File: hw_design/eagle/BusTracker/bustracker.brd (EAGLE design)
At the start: 53.3 x 59.7 mm, 9 parts, among them J1 ARDUINO_R3_SHIELD

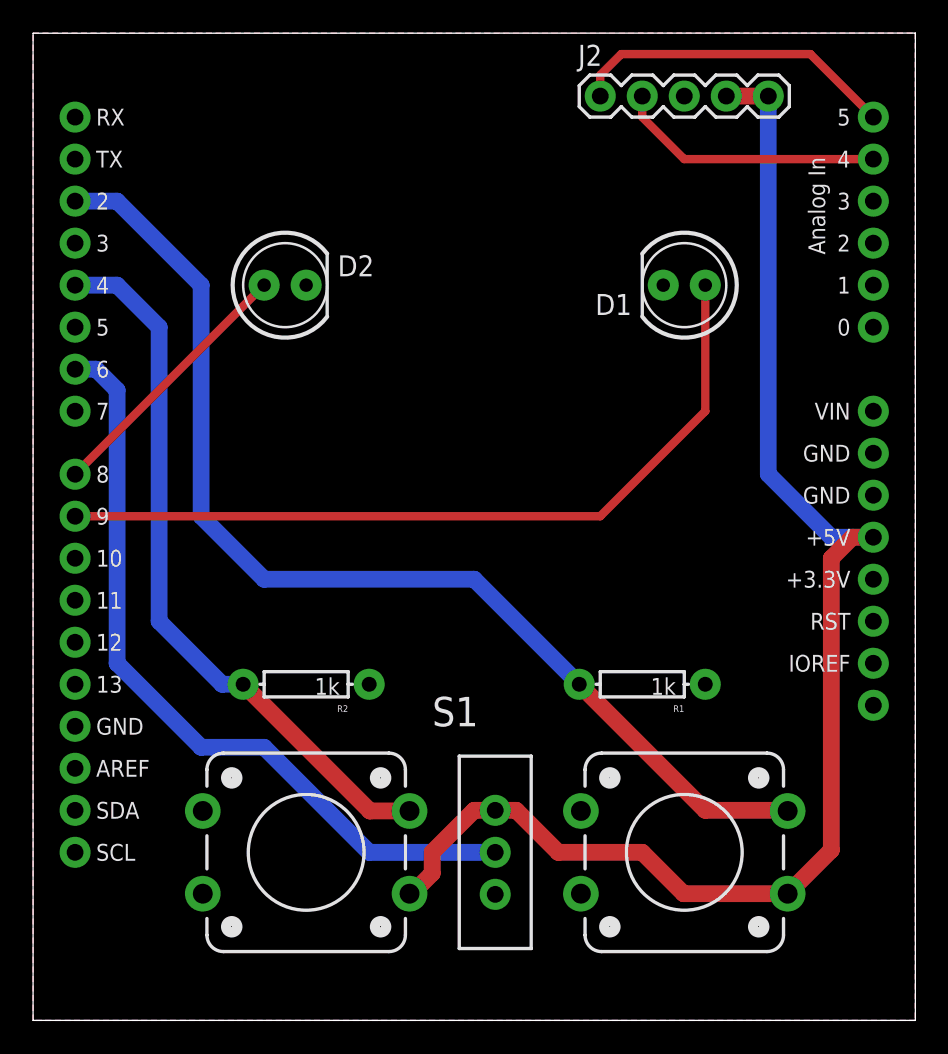
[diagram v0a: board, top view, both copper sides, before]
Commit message: Added silkscreen layer
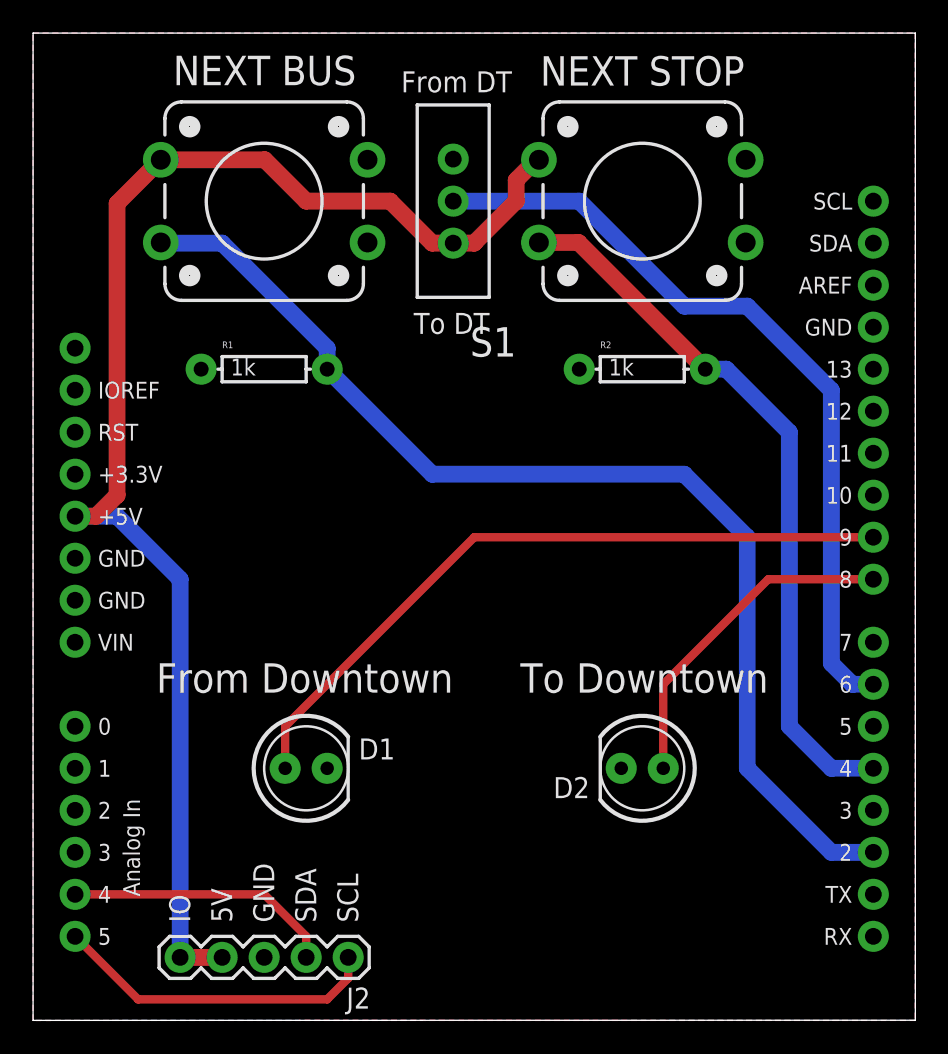
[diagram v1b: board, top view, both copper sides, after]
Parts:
- moved J1 80.1 mm to (53.3, 59.7), turned to 180 degrees
- moved J2 54.3 mm to (19.1, 3.81), turned to 180 degrees
- moved S2 46.9 mm to (14.0, 49.5), turned to 180 degrees
- moved S3 44.3 mm to (36.8, 49.5), turned to 180 degrees
- moved S1 39.5 mm to (25.4, 49.5), turned to 180 degrees
- moved D1 37.1 mm to (16.5, 15.2), turned to 0 degrees
- moved D2 36.3 mm to (36.8, 15.2), turned to 180 degrees
- moved R1 29.8 mm to (14.0, 39.4), turned to 0 degrees
- moved R2 27.9 mm to (36.8, 39.4), turned to 0 degrees
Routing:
- net REDLEDPIN: track 48.4 -> 42.8 mm
- net GREENLEDPIN: track 16.2 -> 20.4 mm
- net NEXTBUS_BTN: track 66.5 -> 67.3 mm
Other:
- board text added: "5V"
- board text added: "From DT"
- board text added: "From Downtown"
- board text added: "GND"
- board text added: "IO"
- board text added: "NEXT BUS"
- board text added: "NEXT STOP"
- board text added: "SCL"
- board text added: "SDA"
- board text added: "To DT"
- board text added: "To Downtown"

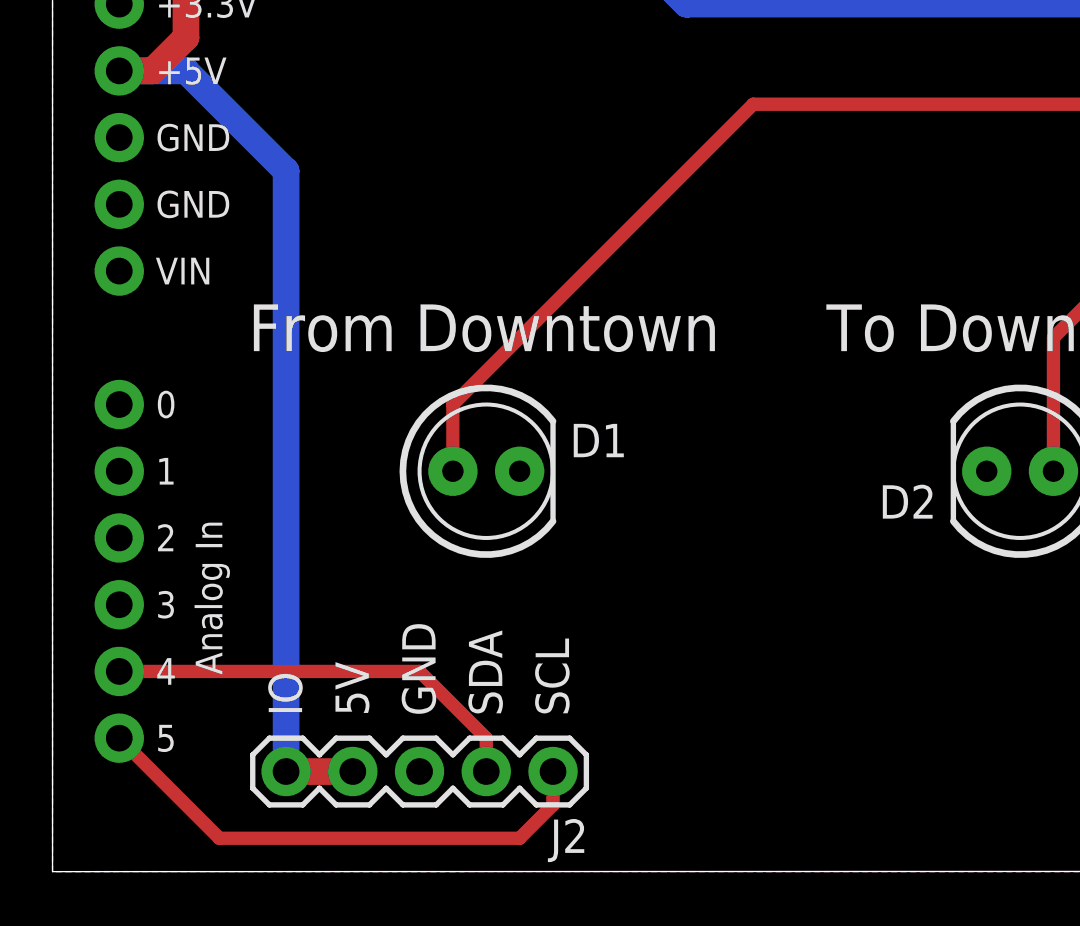
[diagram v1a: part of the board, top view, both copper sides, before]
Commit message: Changed I2C pins position
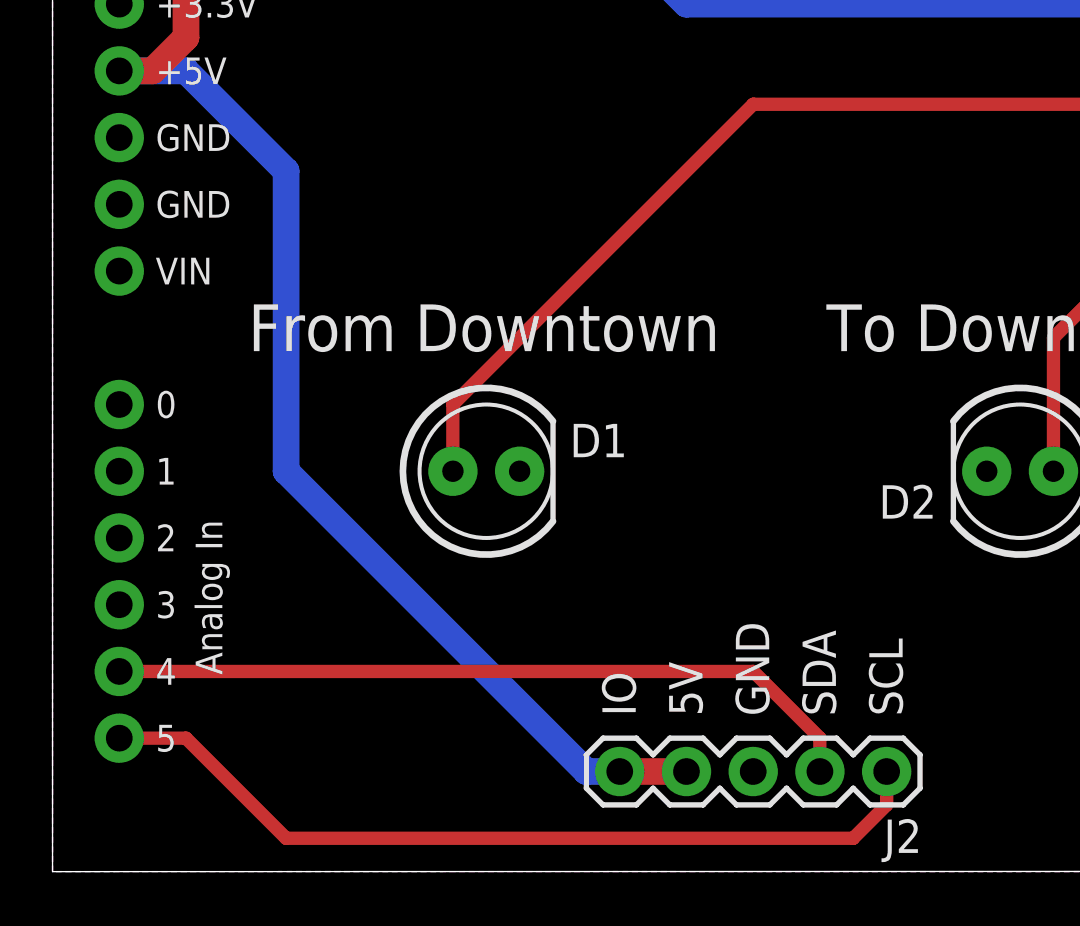
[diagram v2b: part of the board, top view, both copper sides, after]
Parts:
- moved J2 12.7 mm to (31.8, 3.81)
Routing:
- net SDA: track 16.3 -> 29.0 mm
- net SCL: track 19.9 -> 32.6 mm
- net 5V: track 85.5 -> 91.6 mm
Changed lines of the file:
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@@
 <text x="44.45" y="21.59" size="1.778" layer="21" rot="R180">To Downtown</text>
 <text x="25.4" y="21.59" size="1.778" layer="21" rot="R180">From Downtown</text>
-<text x="9.4996" y="5.9182" size="1.27" layer="21" rot="R90">IO</text>
-<text x="12.0396" y="5.9182" size="1.27" layer="21" rot="R90">5V</text>
-<text x="14.5796" y="5.9182" size="1.27" layer="21" rot="R90">GND</text>
-<text x="17.1196" y="5.9182" size="1.27" layer="21" rot="R90">SDA</text>
-<text x="19.6596" y="5.9182" size="1.27" layer="21" rot="R90">SCL</text>
+<text x="22.1996" y="5.9182" size="1.27" layer="21" rot="R90">IO</text>
+<text x="24.7396" y="5.9182" size="1.27" layer="21" rot="R90">5V</text>
+<text x="27.2796" y="5.9182" size="1.27" layer="21" rot="R90">GND</text>
+<text x="29.8196" y="5.9182" size="1.27" layer="21" rot="R90">SDA</text>
+<text x="32.3596" y="5.9182" size="1.27" layer="21" rot="R90">SCL</text>
 <text x="23.0124" y="41.5036" size="1.27" layer="21">To DT</text>
 <text x="22.2504" y="56.1086" size="1.27" layer="21">From DT</text>
@@
 <element name="D1" library="SparkFun-LED" package="LED5MM" value="" x="16.51" y="15.24"/>
 <element name="D2" library="SparkFun-LED" package="LED5MM" value="" x="36.83" y="15.24" rot="R180"/>
-<element name="J2" library="SparkFun-Connectors" package="1X05" value="" x="19.05" y="3.81" rot="R180"/>
+<element name="J2" library="SparkFun-Connectors" package="1X05" value="" x="31.75" y="3.81" rot="R180"/>
 <element name="R1" library="SparkFun-Resistors" package="AXIAL-0.3" value="1k" x="13.97" y="39.37">
 <attribute name="PROD_ID" value="RES-08380" x="13.97" y="39.37" size="1.778" layer="27" display="off"/>
@@
 <contactref element="J1" pad="5V"/>
 <contactref element="J2" pad="5"/>
-<wire x1="11.43" y1="3.81" x2="8.89" y2="3.81" width="1.016" layer="1"/>
+<wire x1="24.13" y1="3.81" x2="21.59" y2="3.81" width="1.016" layer="1"/>
 <wire x1="2.54" y1="30.48" x2="3.81" y2="30.48" width="1.016" layer="1"/>
 <wire x1="3.81" y1="30.48" x2="5.08" y2="31.75" width="1.016" layer="1"/>
@@
 <wire x1="30.58" y1="52.03" x2="30.44" y2="52.03" width="1.016" layer="1"/>
 <wire x1="30.44" y1="52.03" x2="29.21" y2="50.8" width="1.016" layer="1"/>
-<wire x1="8.89" y1="3.81" x2="8.89" y2="26.67" width="1.016" layer="16"/>
+<wire x1="21.59" y1="3.81" x2="20.32" y2="3.81" width="1.016" layer="16"/>
+<wire x1="20.32" y1="3.81" x2="8.89" y2="15.24" width="1.016" layer="16"/>
+<wire x1="8.89" y1="15.24" x2="8.89" y2="26.67" width="1.016" layer="16"/>
 <wire x1="8.89" y1="26.67" x2="5.08" y2="30.48" width="1.016" layer="16"/>
 <wire x1="5.08" y1="30.48" x2="2.54" y2="30.48" width="1.016" layer="16"/>
@@
 <contactref element="J2" pad="2"/>
 <contactref element="J1" pad="A4"/>
-<wire x1="16.51" y1="3.81" x2="16.51" y2="5.08" width="0.508" layer="1"/>
-<wire x1="16.51" y1="5.08" x2="13.97" y2="7.62" width="0.508" layer="1"/>
-<wire x1="13.97" y1="7.62" x2="2.54" y2="7.62" width="0.508" layer="1"/>
+<wire x1="29.21" y1="3.81" x2="29.21" y2="5.08" width="0.508" layer="1"/>
+<wire x1="29.21" y1="5.08" x2="26.67" y2="7.62" width="0.508" layer="1"/>
+<wire x1="26.67" y1="7.62" x2="2.54" y2="7.62" width="0.508" layer="1"/>
 </signal>
 <signal name="SCL">
 <contactref element="J2" pad="1"/>
 <contactref element="J1" pad="A5"/>
-<wire x1="19.05" y1="3.81" x2="19.05" y2="2.54" width="0.508" layer="1"/>
-<wire x1="19.05" y1="2.54" x2="17.78" y2="1.27" width="0.508" layer="1"/>
-<wire x1="17.78" y1="1.27" x2="6.35" y2="1.27" width="0.508" layer="1"/>
-<wire x1="6.35" y1="1.27" x2="2.54" y2="5.08" width="0.508" layer="1"/>
+<wire x1="31.75" y1="3.81" x2="31.75" y2="2.54" width="0.508" layer="1"/>
+<wire x1="31.75" y1="2.54" x2="30.48" y2="1.27" width="0.508" layer="1"/>
+<wire x1="30.48" y1="1.27" x2="8.89" y2="1.27" width="0.508" layer="1"/>
+<wire x1="8.89" y1="1.27" x2="5.08" y2="5.08" width="0.508" layer="1"/>
+<wire x1="5.08" y1="5.08" x2="2.54" y2="5.08" width="0.508" layer="1"/>
 </signal>
 <signal name="NEXTBUS_BTN">
